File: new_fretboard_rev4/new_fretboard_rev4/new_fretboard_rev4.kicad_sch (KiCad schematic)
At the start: 56 parts, among them CN1 Header 1x6, CN2 Header 1x6, J1 JMP, J2 JMP, J3 JMP, J4 JMP, J5 JMP, J6 JMP, J7 JMP, J8 JMP, U1 LX3302AQPW_TSSOP-14, U2 LX3302AQPW_TSSOP-14

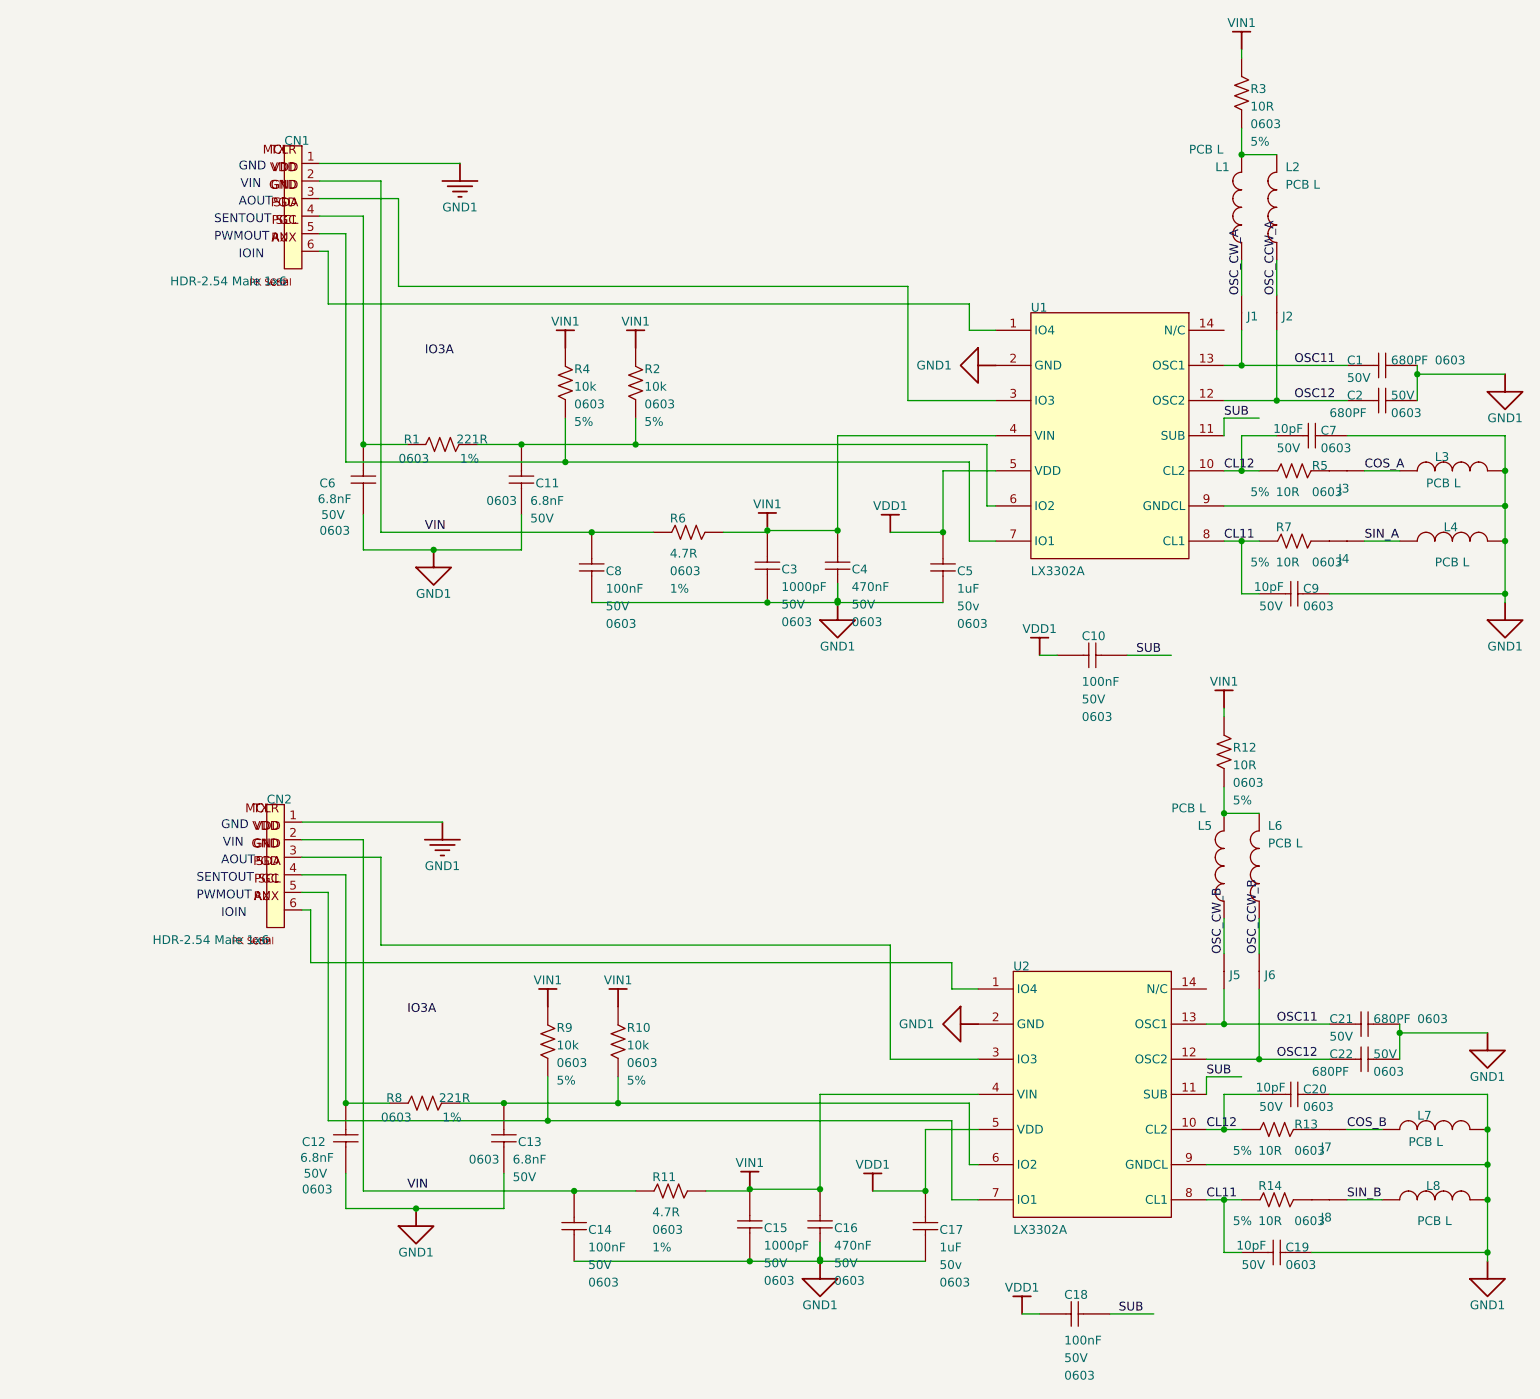
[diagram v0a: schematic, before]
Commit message: updating net names of rest of circuit
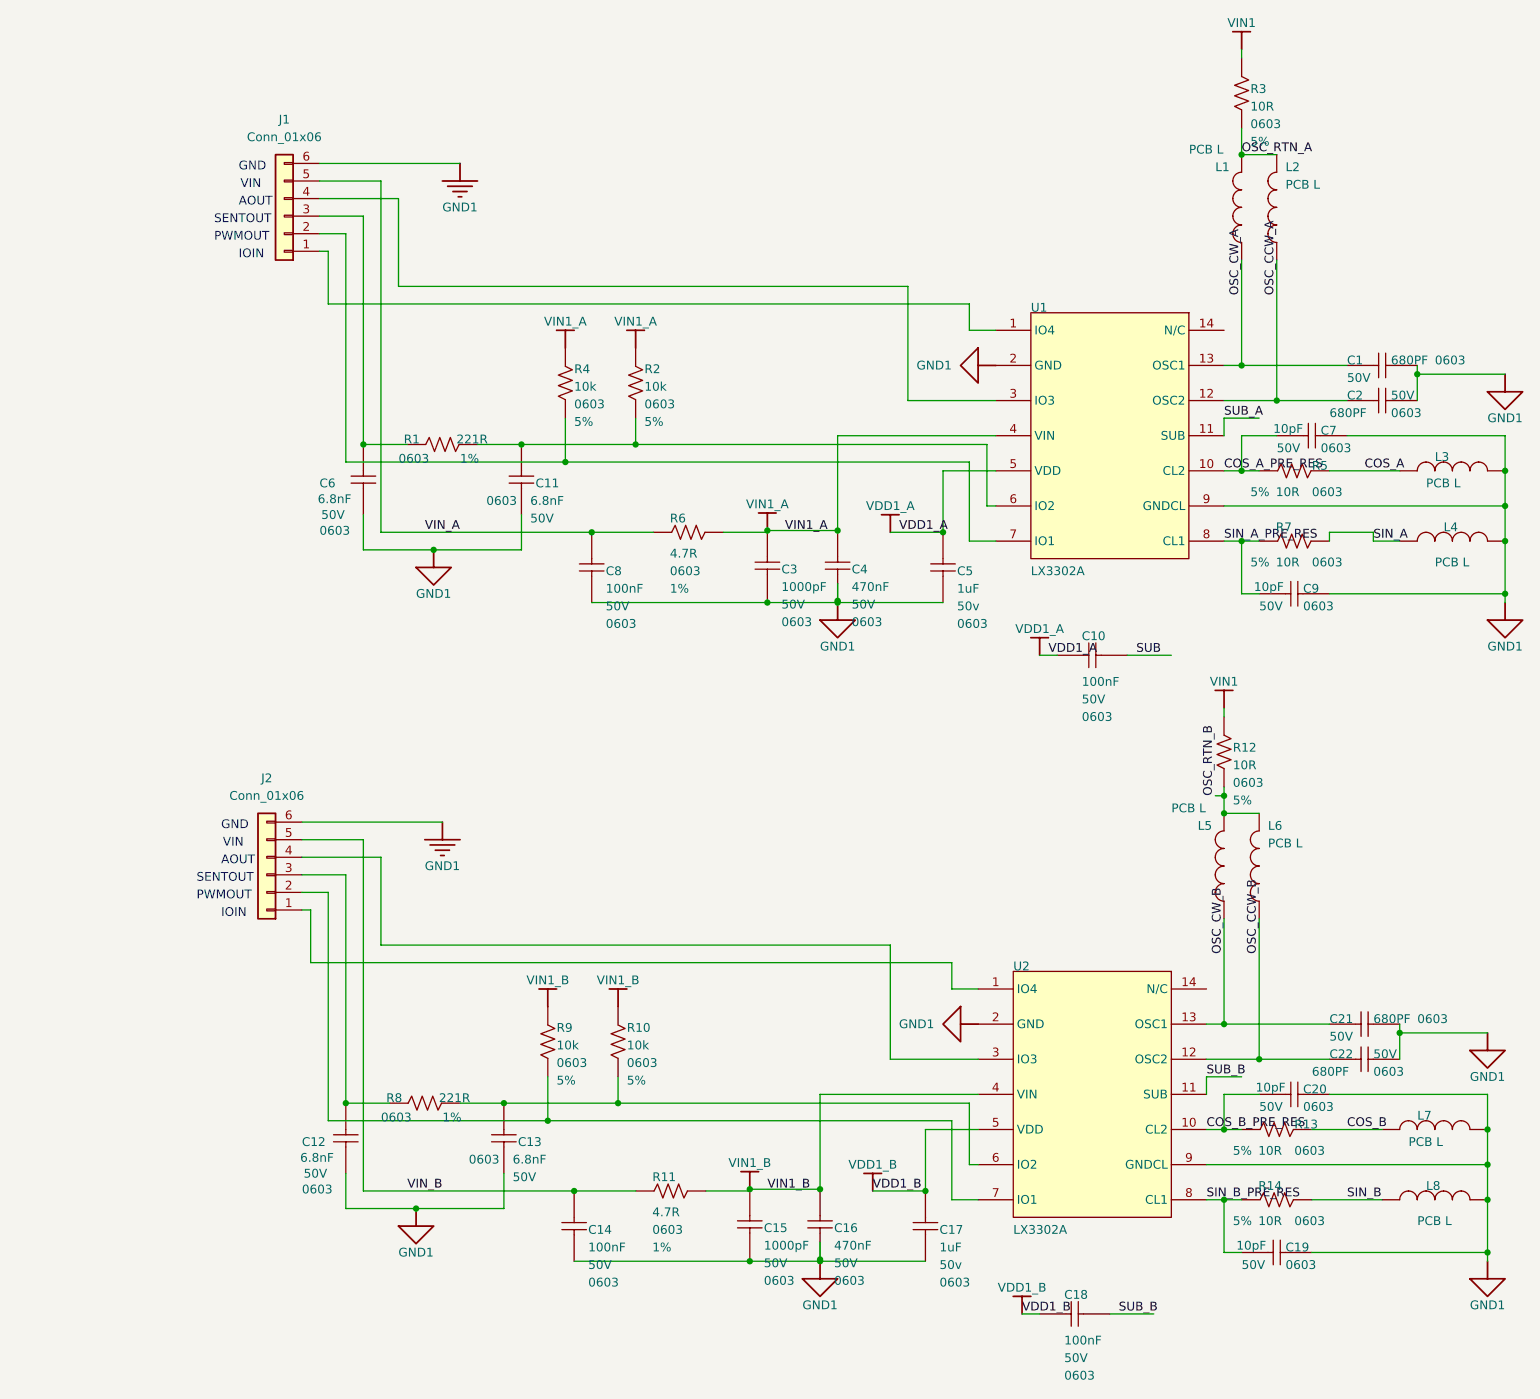
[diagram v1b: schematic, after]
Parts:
- removed CN1, CN2: Header 1x6, HDR_M_2.54_1x6, symbol MCHP-CDB:root_3_Header 1x6_MCHP-CDB.DbLib_0
- removed J1, J2, J5, J6: JMP, JMP, symbol LX3301EVB1R1X1:root_0_JMP_LX3301EVB1R1X1.SCHLIB
- removed J3, J4, J7, J8: JMP, JMP, symbol LX3301EVB1R1X1:root_1_JMP_LX3301EVB1R1X1.SCHLIB
- added J1, J2: Conn_01x06, 4ms_Connector:Pins_1x06_2.54mm_TH_SWD, symbol PCM_4ms_Connector:Conn_01x06
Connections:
- net COS_A: now also R5.2
- net COS_B: now also R13.2
- net GND1: now also J1.6 (Pin_6), J2.6 (Pin_6)
- net OSC_CCW_A: now also C2.2, U1.12 (OSC2)
- net OSC_CCW_B: now also C22.2, U2.12 (OSC2)
- net OSC_CW_A: now also C1.2, U1.13 (OSC1)
- net OSC_CW_B: now also C21.2, U2.13 (OSC1)
- net SIN_A: now also R7.2
- net SIN_B: now also R14.2
- net SUB: no longer C18.1, U1.11 (SUB), U2.11 (SUB)
- net VIN1: no longer C15.2, C16.2, C3.2, C4.2, R10.2, R11.2, R2.2, R4.2, R6.2, R9.2, U1.4 (VIN), U2.4 (VIN)
- net at C12.2, R8.1: now also J2.3 (Pin_3)
- net OSC_RTN_A: now reaches L1.2, L2.2, R3.1
- net at U2.1 (IO4): now also J2.1 (Pin_1)
- net at U2.3 (IO3): now also J2.4 (Pin_4)
- net at R9.1, U2.7 (IO1): now also J2.2 (Pin_2)
- net at C6.2, R1.1: now also J1.3 (Pin_3)
- net OSC_RTN_B: now reaches L5.2, L6.2, R12.1
- net at U1.3 (IO3): now also J1.4 (Pin_4)
- net at R4.1, U1.7 (IO1): now also J1.2 (Pin_2)
- net at U1.1 (IO4): now also J1.1 (Pin_1)
- net CL11 renamed SIN_A_PRE_RES
- net SIN_A_PRE_RES: no longer C19.2, R14.1, U2.8 (CL1)
- net CL12 renamed COS_A_PRE_RES
- net COS_A_PRE_RES: no longer C20.2, R13.1, U2.10 (CL2)
- removed net OSC11: C1.2, C21.2, U1.13 (OSC1), U2.13 (OSC1)
- removed net OSC12: C2.2, C22.2, U1.12 (OSC2), U2.12 (OSC2)
- net VDD1 renamed VDD1_A
- net VDD1_A: no longer C17.2, C18.2, U2.5 (VDD)
- net VIN renamed VIN_A
- net VIN_A: now also J1.5 (Pin_5); no longer C14.2, R11.1
- new net COS_B_PRE_RES: C20.2, R13.1, U2.10 (CL2)
- new net SIN_B_PRE_RES: C19.2, R14.1, U2.8 (CL1)
- new net SUB_A: U1.11 (SUB)
- new net SUB_B: C18.1, U2.11 (SUB)
- new net VDD1_B: C17.2, C18.2, U2.5 (VDD)
- new net VIN1_A: C3.2, C4.2, R2.2, R4.2, R6.2, U1.4 (VIN)
- new net VIN1_B: C15.2, C16.2, R10.2, R11.2, R9.2, U2.4 (VIN)
- new net VIN_B: C14.2, J2.5 (Pin_5), R11.1

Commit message: part footprints chosen
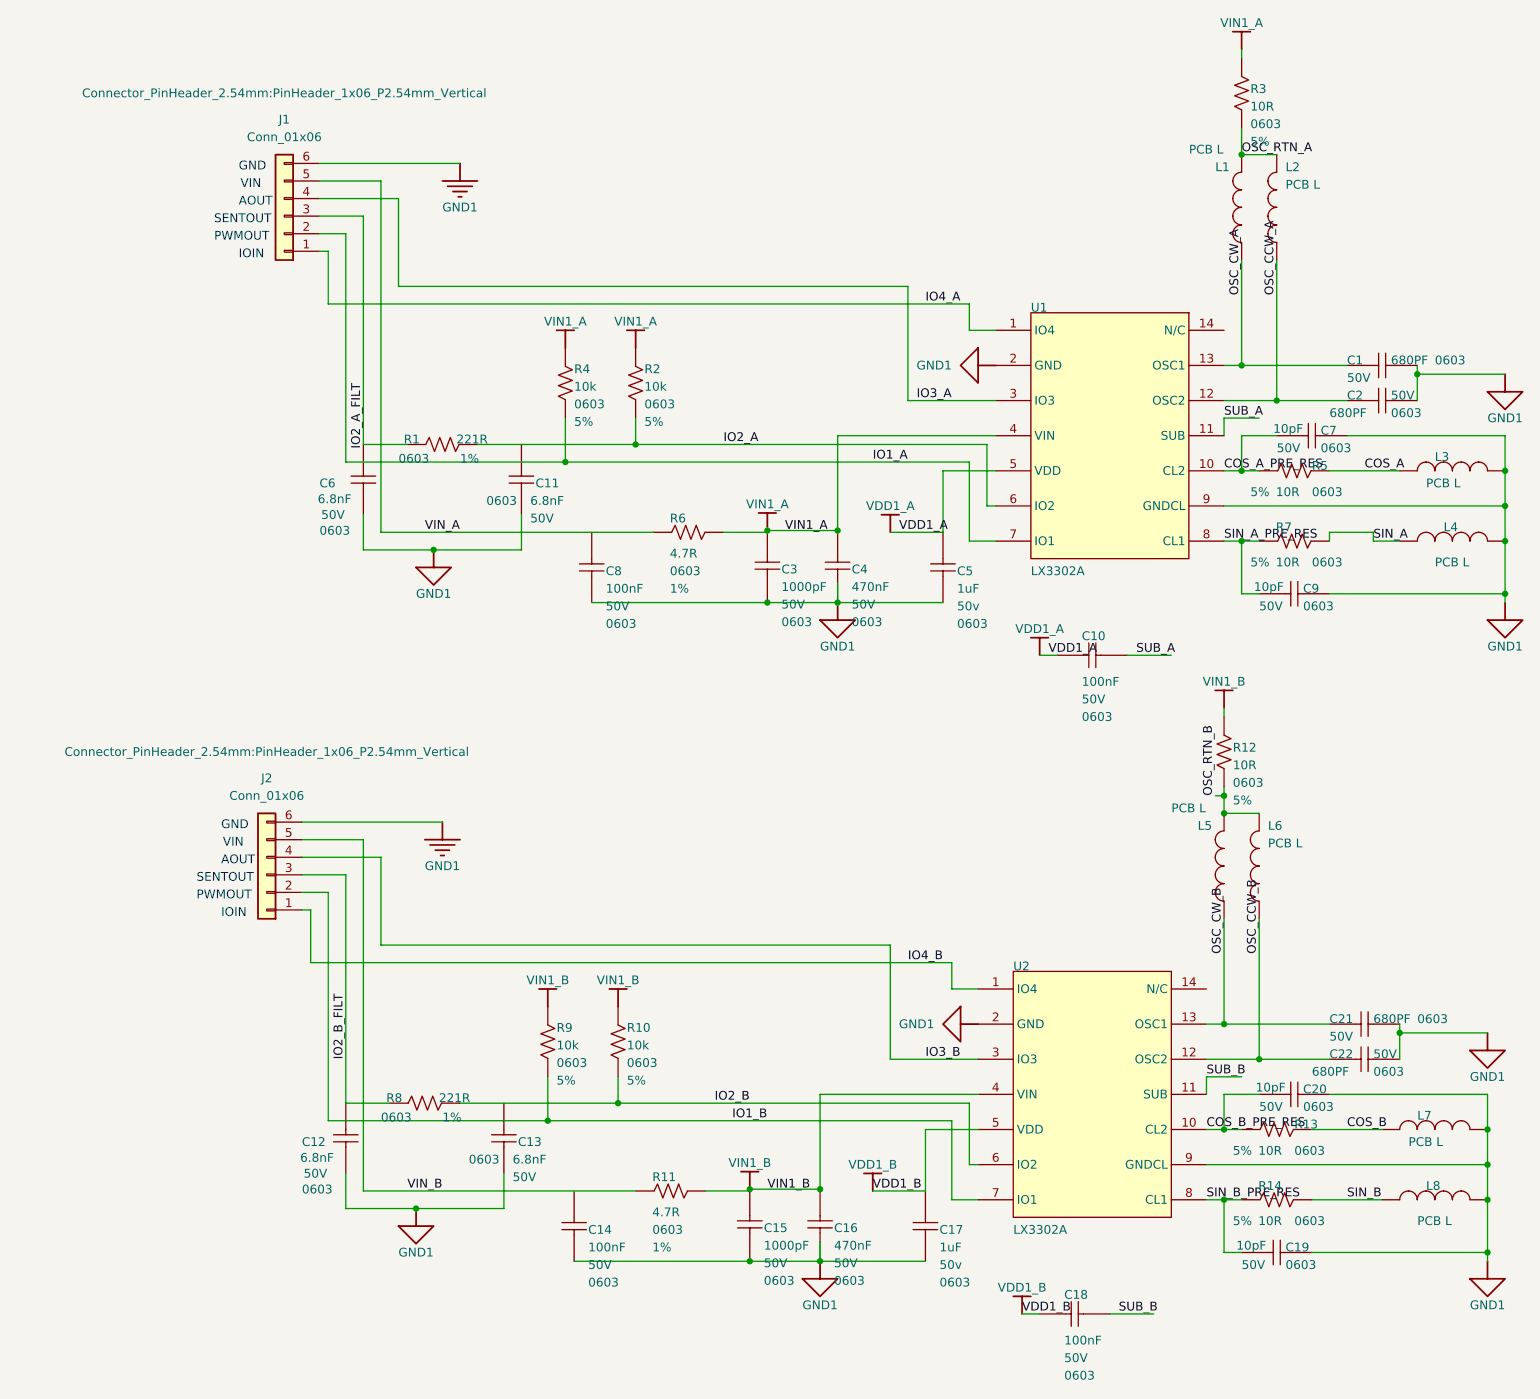
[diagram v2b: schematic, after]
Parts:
- C1, C10, C11, C12, C13, C14, C15, C16, C17, C18, C19, C2, C20, C21, C22, C3, C4, C5, C6, C7, C8, C9: footprint CAP_C_0603 -> PCM_4ms_Capacitor:C_0603
- J1, J2: footprint 4ms_Connector:Pins_1x06_2.54mm_TH_SWD -> Connector_PinHeader_2.54mm:PinHeader_1x06_P2.54mm_Vertical
- R1, R10, R11, R12, R13, R14, R2, R3, R4, R5, R6, R7, R8, R9: footprint RES_C_0603 -> PCM_4ms_Resistor:R_0603
- U1, U2: footprint TSSOP-14 -> PCM_4ms_Package_SSOP:TSSOP-14_4.4x5mm_P0.65mm
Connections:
- net SUB is gone; now on net SUB_A: C10.1
- net GND1: no longer C16.1, C4.1
- net VIN1_A: now also R3.2
- net VIN1_B: now also R12.2
- net VIN_A: no longer C8.2
- net VIN_B: no longer C14.2
- net IO2_B_FILT: now reaches C12.2, J2.3 (Pin_3), R8.1
- net IO2_A: now reaches R1.2, R2.1, U1.6 (IO2)
- net IO2_A: no longer C11.2
- net IO2_B: now reaches R10.1, R8.2, U2.6 (IO2)
- net IO2_B: no longer C13.2
- net IO4_B: now reaches J2.1 (Pin_1), U2.1 (IO4)
- net IO3_B: now reaches J2.4 (Pin_4), U2.3 (IO3)
- net IO1_B: now reaches J2.2 (Pin_2), R9.1, U2.7 (IO1)
- net IO2_A_FILT: now reaches C6.2, J1.3 (Pin_3), R1.1
- net IO4_A: now reaches J1.1 (Pin_1), U1.1 (IO4)
- net IO3_A: now reaches J1.4 (Pin_4), U1.3 (IO3)
- net IO1_A: now reaches J1.2 (Pin_2), R4.1, U1.7 (IO1)
- removed net VIN1: R12.2, R3.2

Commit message: added new footprint jumpers
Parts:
- L1, L2, L5, L6, L7, L8: footprint JMP -> jumpers_custom:jumper_tiny
- L3, L4: footprint NetTie:NetTie-2_SMD_Pad0.5mm -> jumpers_custom:jumper_tiny
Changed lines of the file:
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@@
 			)
 		)
-		(property "Footprint" "NetTie:NetTie-2_SMD_Pad0.5mm"
+		(property "Footprint" "jumpers_custom:jumper_tiny"
 			(at 210.82 101.6 0)
 			(effects
@@
 			)
 		)
-		(property "Footprint" "JMP"
+		(property "Footprint" "jumpers_custom:jumper_tiny"
 			(at 187.96 60.96 0)
 			(effects
@@
 			)
 		)
-		(property "Footprint" "NetTie:NetTie-2_SMD_Pad0.5mm"
+		(property "Footprint" "jumpers_custom:jumper_tiny"
 			(at 210.82 91.44 0)
 			(effects
@@
 			)
 		)
-		(property "Footprint" "JMP"
+		(property "Footprint" "jumpers_custom:jumper_tiny"
 			(at 185.42 156.21 0)
 			(effects
@@
 			)
 		)
-		(property "Footprint" "JMP"
+		(property "Footprint" "jumpers_custom:jumper_tiny"
 			(at 208.28 186.69 0)
 			(effects
@@
 			)
 		)
-		(property "Footprint" "JMP"
+		(property "Footprint" "jumpers_custom:jumper_tiny"
 			(at 182.88 60.96 0)
 			(effects
@@
 			)
 		)
-		(property "Footprint" "JMP"
+		(property "Footprint" "jumpers_custom:jumper_tiny"
 			(at 180.34 156.21 0)
 			(effects
@@
 			)
 		)
-		(property "Footprint" "JMP"
+		(property "Footprint" "jumpers_custom:jumper_tiny"
 			(at 208.28 196.85 0)
 			(effects

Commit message: partway through routing top
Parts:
- C1, C2, C21, C22: value Capacitor NP -> 680PF
- C10, C14, C18, C8: value Capacitor NP -> 100nF
- C11, C12, C13, C6: value Capacitor NP -> 6.8nF
- C15, C3: value Capacitor NP -> 1000pF
- C16, C4: value Capacitor NP -> 470nF
- C17, C5: value Capacitor NP -> 1uF
- C19, C20, C7, C9: value Capacitor NP -> 10pF
- R1, R8: value Resistor -> 221R
- R10, R2, R4, R9: value Resistor -> 10k
- R11, R6: value Resistor -> 4.7R
- R12, R13, R14, R3, R5, R7: value Resistor -> 10R
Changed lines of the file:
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@@
 			)
 		)
-		(property "Value" "Capacitor NP"
+		(property "Value" "680PF"
 			(at 200.152 76.708 0)
 			(effects
@@
 				)
 				(justify left bottom)
-				(hide yes)
 			)
 		)
@@
 			)
 		)
-		(property "Value" "Capacitor NP"
+		(property "Value" "6.8nF"
 			(at 53.848 184.912 0)
 			(effects
@@
 			)
 		)
-		(property "Value" "Capacitor NP"
+		(property "Value" "470nF"
 			(at 124.968 102.108 0)
 			(effects
@@
 			)
 		)
-		(property "Value" "Resistor"
+		(property "Value" "10R"
 			(at 184.15 203.2 0)
 			(effects
@@
 			)
 		)
-		(property "Value" "Capacitor NP"
+		(property "Value" "1uF"
 			(at 140.208 102.362 0)
 			(effects
@@
 			)
 		)
-		(property "Value" "Resistor"
+		(property "Value" "10k"
 			(at 96.52 75.692 0)
 			(effects
@@
 			)
 		)
-		(property "Value" "Capacitor NP"
+		(property "Value" "100nF"
 			(at 155.702 213.868 0)
 			(effects
@@
 			)
 		)
-		(property "Value" "Capacitor NP"
+		(property "Value" "6.8nF"
 			(at 76.708 184.912 0)
 			(effects
@@
 			)
 		)
-		(property "Value" "Capacitor NP"
+		(property "Value" "100nF"
 			(at 89.408 102.362 0)
 			(effects
@@
 			)
 		)
-		(property "Value" "Capacitor NP"
+		(property "Value" "6.8nF"
 			(at 56.388 89.662 0)
 			(effects
@@
 			)
 		)
-		(property "Value" "Capacitor NP"
+		(property "Value" "680PF"
 			(at 197.612 177.038 0)
 			(effects
@@
 			)
 		)
-		(property "Value" "Capacitor NP"
+		(property "Value" "6.8nF"
 			(at 79.248 89.662 0)
 			(effects
@@
 			)
 		)
-		(property "Value" "Resistor"
+		(property "Value" "4.7R"
 			(at 96.52 201.93 0)
 			(effects
@@
 			)
 		)
-		(property "Value" "Capacitor NP"
+		(property "Value" "10pF"
 			(at 189.992 86.868 0)
 			(effects
@@
 			)
 		)
-		(property "Value" "Resistor"
+		(property "Value" "10R"
 			(at 184.15 33.782 0)
 			(effects
@@
 			)
 		)
-		(property "Value" "Capacitor NP"
+		(property "Value" "100nF"
 			(at 158.242 118.618 0)
 			(effects
@@
 			)
 		)
-		(property "Value" "Resistor"
+		(property "Value" "10R"
 			(at 186.69 107.95 0)
 			(effects
@@
 			)
 		)
-		(property "Value" "Capacitor NP"
+		(property "Value" "1000pF"
 			(at 114.808 102.108 0)
 			(effects
@@
 			)
 		)
-		(property "Value" "Resistor"
+		(property "Value" "10R"
 			(at 181.61 129.032 0)
 			(effects
@@
 			)
 		)
-		(property "Value" "Capacitor NP"
+		(property "Value" "680PF"
 			(at 197.612 171.958 0)
 			(effects
@@
 			)
 		)
-		(property "Value" "Resistor"
+		(property "Value" "4.7R"
 			(at 99.06 106.68 0)
 			(effects
@@
 			)
 		)
-		(property "Value" "Resistor"
+		(property "Value" "221R"
 			(at 60.96 189.23 0)
 			(effects
@@
 			)
 		)
-		(property "Value" "Capacitor NP"
+		(property "Value" "10pF"
 			(at 187.452 109.728 0)
 			(effects
@@
 				)
 				(justify left bottom)
-				(hide yes)
 			)
 		)
@@
 			)
 		)
-		(property "Value" "Capacitor NP"
+		(property "Value" "1000pF"
 			(at 112.268 197.358 0)
 			(effects
@@
 			)
 		)
-		(property "Value" "Resistor"
+		(property "Value" "221R"
 			(at 63.5 93.98 0)
 			(effects
@@
 			)
 		)
-		(property "Value" "Resistor"
+		(property "Value" "10k"
 			(at 93.98 170.942 0)
 			(effects
@@
 			)
 		)
-		(property "Value" "Resistor"
+		(property "Value" "10R"
 			(at 184.15 193.04 0)
 			(effects
@@
 			)
 		)
-		(property "Value" "Capacitor NP"
+		(property "Value" "470nF"
 			(at 122.428 197.358 0)
 			(effects
@@
 			)
 		)
-		(property "Value" "Resistor"
+		(property "Value" "10R"
 			(at 186.69 97.79 0)
 			(effects
@@
 				)
 				(justify left bottom)
-				(hide yes)
 			)
 		)
@@
 			)
 		)
-		(property "Value" "Resistor"
+		(property "Value" "10k"
 			(at 86.36 75.692 0)
 			(effects
@@
 			)
 		)
-		(property "Value" "Capacitor NP"
+		(property "Value" "1uF"
 			(at 137.668 197.612 0)
 			(effects
@@
 			)
 		)
-		(property "Value" "Capacitor NP"
+		(property "Value" "100nF"
 			(at 86.868 197.612 0)
 			(effects
@@
 			)
 		)
-		(property "Value" "Capacitor NP"
+		(property "Value" "10pF"
 			(at 184.912 204.978 0)
 			(effects
@@
 			)
 		)
-		(property "Value" "Resistor"
+		(property "Value" "10k"
 			(at 83.82 170.942 0)
 			(effects
@@
 			)
 		)
-		(property "Value" "Capacitor NP"
+		(property "Value" "10pF"
 			(at 187.452 182.118 0)
 			(effects
@@
 			)
 		)
-		(property "Value" "Capacitor NP"
+		(property "Value" "680PF"
 			(at 200.152 81.788 0)
 			(effects
@@
 				)
 				(justify left bottom)
-				(hide yes)
 			)
 		)
